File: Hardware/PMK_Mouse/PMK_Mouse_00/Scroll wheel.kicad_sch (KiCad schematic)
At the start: 2 parts, among them U5 MA702GQ-P, U6 MP6543HGL-P_sch

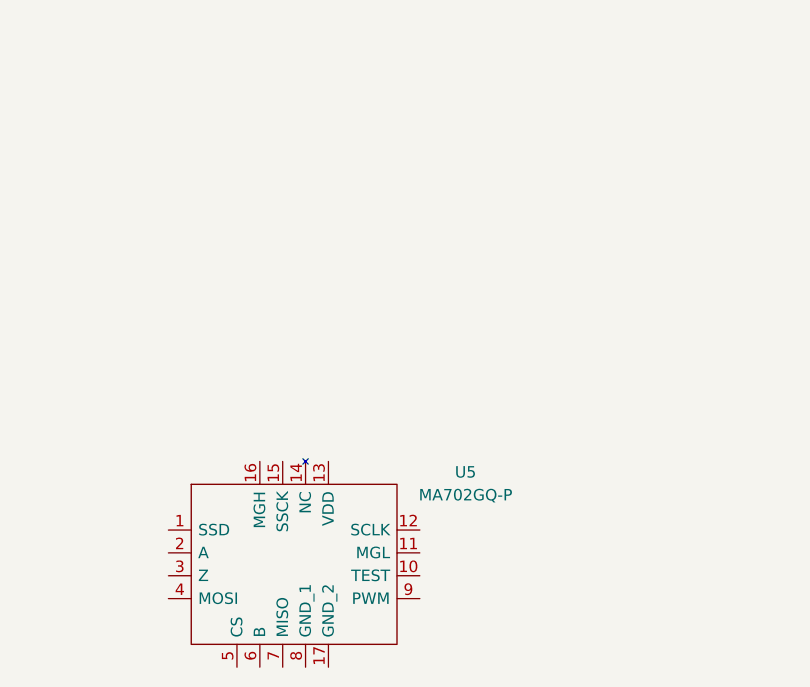
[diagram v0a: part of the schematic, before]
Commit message: touched scroll wheel
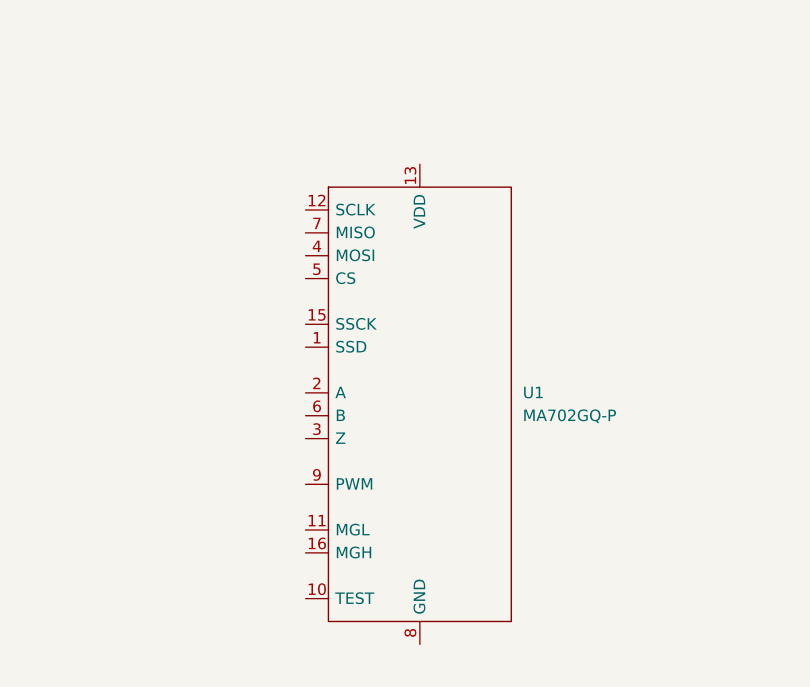
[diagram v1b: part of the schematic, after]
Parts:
- removed U5: MA702GQ-P, Component_lib:QFN50P300X300X100-17N-D, symbol Component_lib:MA702GQ-P
- added U1: MA702GQ-P, Component_lib:QFN50P300X300X100-17N-D, symbol Sensor_lib:MA702GQ-P_sch
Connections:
- new net: U1.17 (GND_2), U1.8 (GND)
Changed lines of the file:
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@@
 	)
 	(symbol
-		(lib_id "Component_lib:MA702GQ-P")
-		(at 144.78 111.76 0)
+		(lib_id "Sensor_lib:MA702GQ-P_sch")
+		(at 160.02 76.2 0)
 		(unit 1)
 		(exclude_from_sim no)
@@
 		(dnp no)
 		(fields_autoplaced yes)
-		(property "Reference" "U5"
-			(at 177.8 105.3398 0)
+		(property "Reference" "U1"
+			(at 184.15 96.5199 0)
 			(effects
 				(font
 					(size 1.27 1.27)
 				)
+				(justify left)
 			)
 		)
 		(property "Value" "MA702GQ-P"
-			(at 177.8 107.8798 0)
+			(at 184.15 99.0599 0)
 			(effects
 				(font
 					(size 1.27 1.27)
 				)
+				(justify left)
 			)
 		)
 		(property "Footprint" "Component_lib:QFN50P300X300X100-17N-D"
-			(at 176.53 83.82 0)
+			(at 191.77 48.26 0)
 			(effects
 				(font
@@
 			)
 		)
-		(property "Datasheet" "https://www.monolithicpower.com/pub/media/document/m/a/ma702_r1.0.pdf"
-			(at 176.53 86.36 0)
+		(property "Datasheet" "https://www.mouser.ch/ProductDetail/Monolithic-Power-Systems-MPS/MA702GQ-P?qs=YCa%2FAAYMW00G2PoyJvHwYg%3D%3D"
+			(at 191.77 50.8 0)
 			(effects
 				(font
@@
 		)
 		(property "Description" "Board Mount Hall Effect / Magnetic Sensors 12-bit, digital, contactless angle sensor with ABZ incremental & PWM outputs"
-			(at 176.53 88.9 0)
+			(at 191.77 53.34 0)
 			(effects
 				(font
@@
 		)
 		(property "Height" "1"
-			(at 176.53 91.44 0)
+			(at 191.77 55.88 0)
 			(effects
 				(font
@@
 		)
 		(property "Mouser Part Number" "946-MA702GQ-P"
-			(at 176.53 93.98 0)
+			(at 191.77 58.42 0)
 			(effects
 				(font
@@
 		)
 		(property "Mouser Price/Stock" "https://www.mouser.co.uk/ProductDetail/Monolithic-Power-Systems-MPS/MA702GQ-P?qs=YCa%2FAAYMW00G2PoyJvHwYg%3D%3D"
-			(at 176.53 96.52 0)
+			(at 191.77 60.96 0)
 			(effects
 				(font
@@
 		)
 		(property "Manufacturer_Name" "Monolithic Power Systems (MPS)"
-			(at 176.53 99.06 0)
+			(at 191.77 63.5 0)
 			(effects
 				(font
@@
 		)
 		(property "Manufacturer_Part_Number" "MA702GQ-P"
-			(at 176.53 101.6 0)
+			(at 191.77 66.04 0)
 			(effects
 				(font
@@
 			)
 		)
-		(pin "12"
-		)
-		(pin "13"
-		)
-		(pin "1"
-		)
 		(pin "15"
-		)
-		(pin "4"
 		)
 		(pin "16"
@@
 		(pin "14"
 		)
+		(pin "6"
+		)
+		(pin "5"
+		)
+		(pin "17"
+		)
+		(pin "2"
+		)
+		(pin "12"
+		)
+		(pin "4"
+		)
+		(pin "11"
+		)
 		(pin "10"
 		)
 		(pin "7"
 		)
-		(pin "17"
+		(pin "1"
 		)
-		(pin "11"
+		(pin "3"
 		)
 		(pin "9"
 		)
-		(pin "5"
-		)
-		(pin "2"
+		(pin "13"
 		)
 		(pin "8"
 		)
-		(pin "3"
-		)
-		(pin "6"
-		)
 		(instances
-			(project "PMK_Mouse_00"
+			(project ""
 				(path "/593534a4-5317-4957-a7cc-7618c0a16adb/b45e4b93-2f01-44f0-a389-f3367ea4f92c"
-					(reference "U5")
+					(reference "U1")
 					(unit 1)
 				)
